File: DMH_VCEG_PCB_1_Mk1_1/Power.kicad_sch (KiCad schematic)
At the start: 71 parts, among them J100 IDC_02x08, J23 Conn_01x10_PinHeader, J27 Conn_01x10_PinHeader, U1 TL074, U10 TL074, U11 TL074, U12 4001, U13 40106, U14 CD4066BE, U15 TL074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

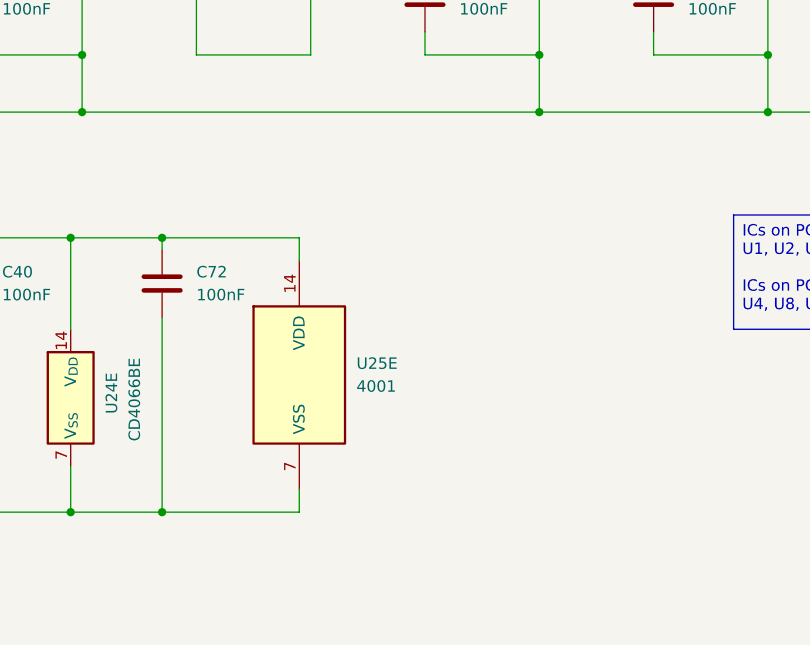
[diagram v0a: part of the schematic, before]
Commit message: Copied Out R redesign to Circuit B
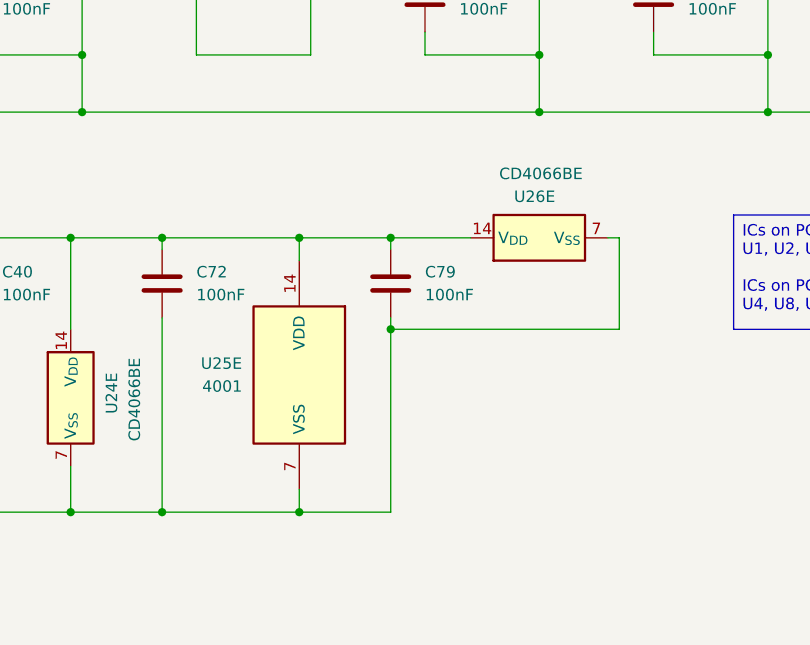
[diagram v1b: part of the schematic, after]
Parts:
- added C79: 100nF, Capacitor_THT:C_Disc_D4.3mm_W1.9mm_P5.00mm, symbol Device:C
- added U26: CD4066BE, Package_DIP:DIP-14_W7.62mm_Socket, symbol Analog_Switch:CD4066BE
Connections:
- net +12V: now also C79.1, U26.14 (V_{DD})
- net GND: now also C79.2, U26.7 (V_{SS})
